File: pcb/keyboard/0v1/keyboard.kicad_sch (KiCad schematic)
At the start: 140 parts, among them SW1 A, SW10 A, SW11 A, SW12 A, SW13 A, SW14 A, SW15 A, SW16 A, SW17 A, SW18 A, SW19 A, SW2 A, SW20 A, SW21 A, SW22 A, SW23 A, SW24 A, SW25 A, SW26 A, SW27 A, SW28 A, SW29 A, SW3 A, SW30 A, SW31 A, SW32 A, SW33 A, SW34 A, SW35 A, SW36 A, SW37 A, SW38 A, SW39 A, SW4 A, SW40 A, SW41 A, SW42 A, SW43 A, SW44 A, SW45 A, SW46 A, SW47 A, SW48 A, SW49 A, SW5 A, SW50 A, SW51 A, SW52 A, SW53 A, SW54 A, SW55 A, SW56 A, SW57 A, SW58 A, SW59 A, SW6 A, SW60 A, SW61 A, SW62 A, SW63 A, SW7 A, SW8 A, SW9 A, U2 MDBT50Q-P1MV2, Y1 32.768

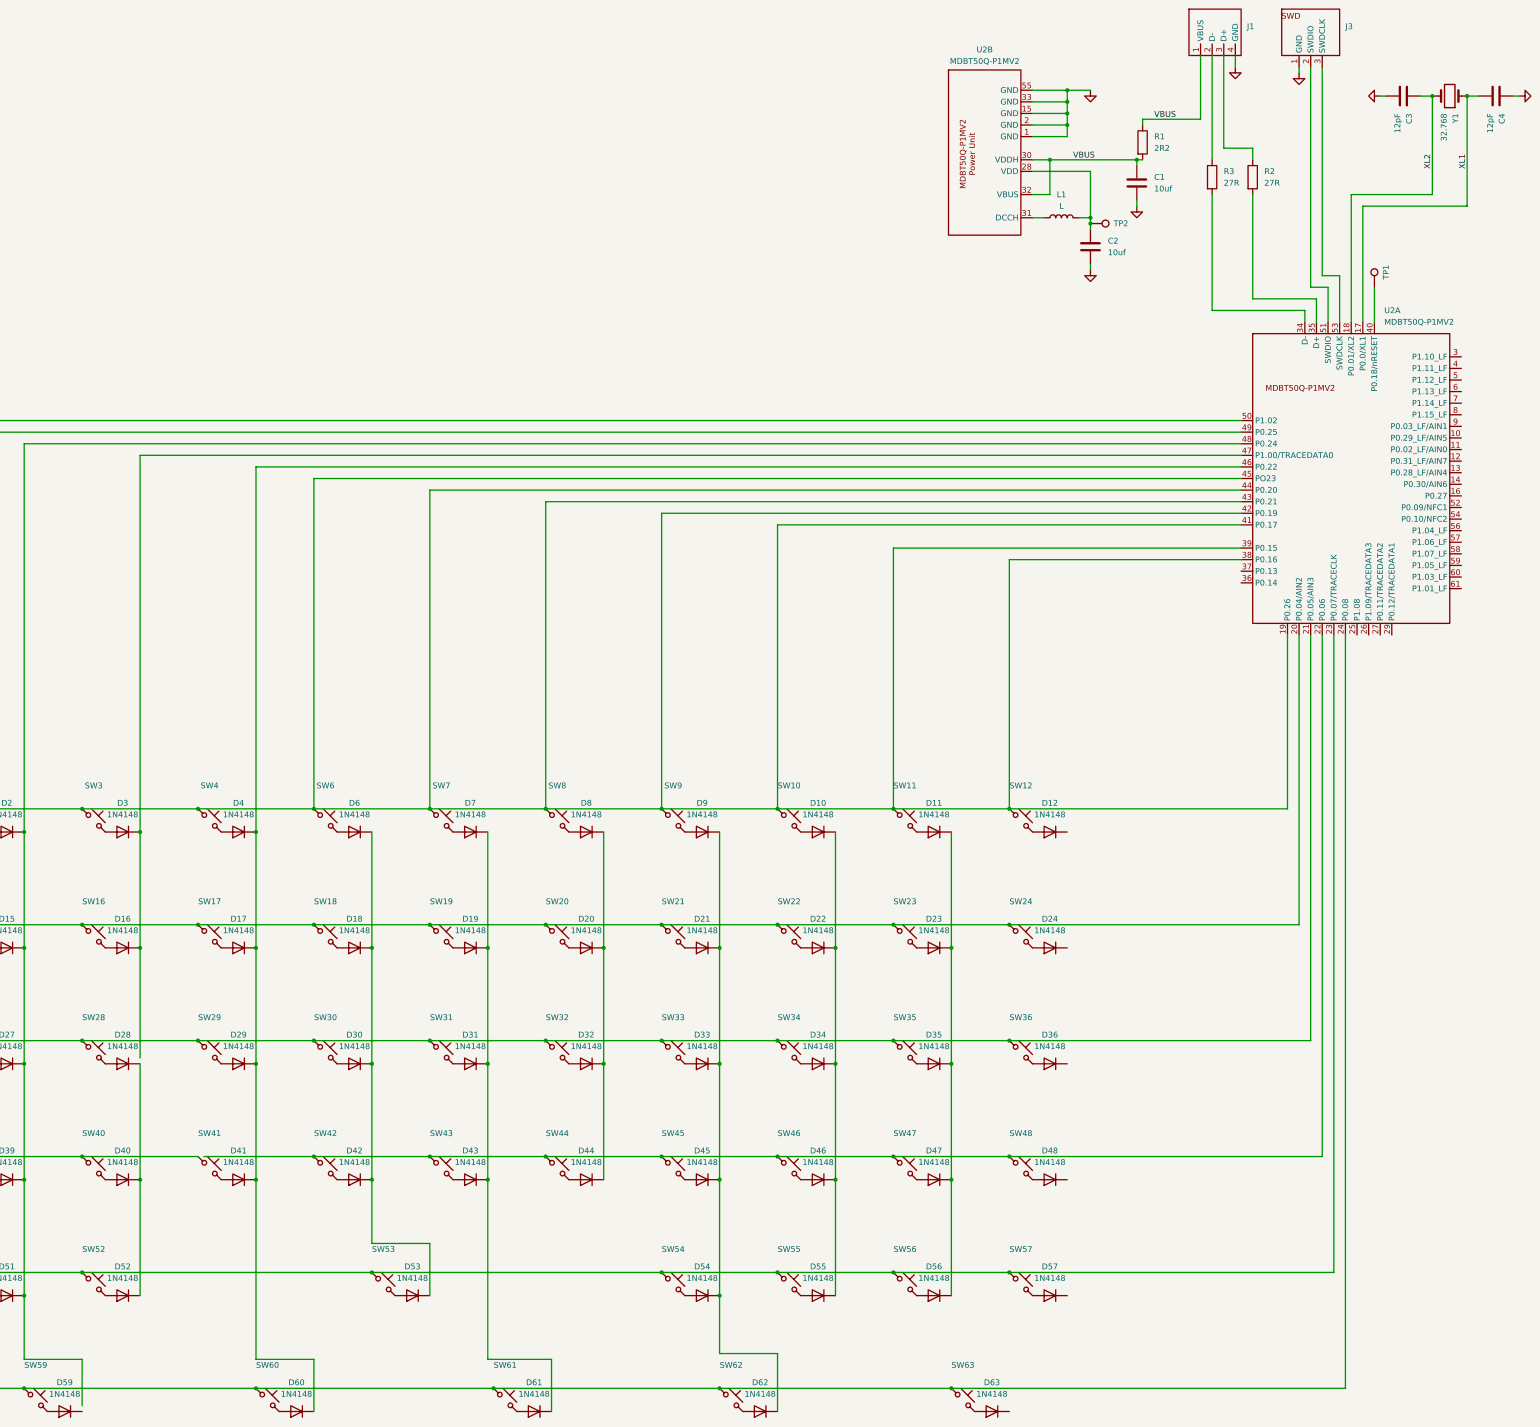
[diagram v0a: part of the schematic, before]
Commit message: Fix ERC errors in schematic editor
There were a few errors with the earlier design. Both real errors and
some just to make the ERC happy. These are fixed now, no errors and no
warnings.
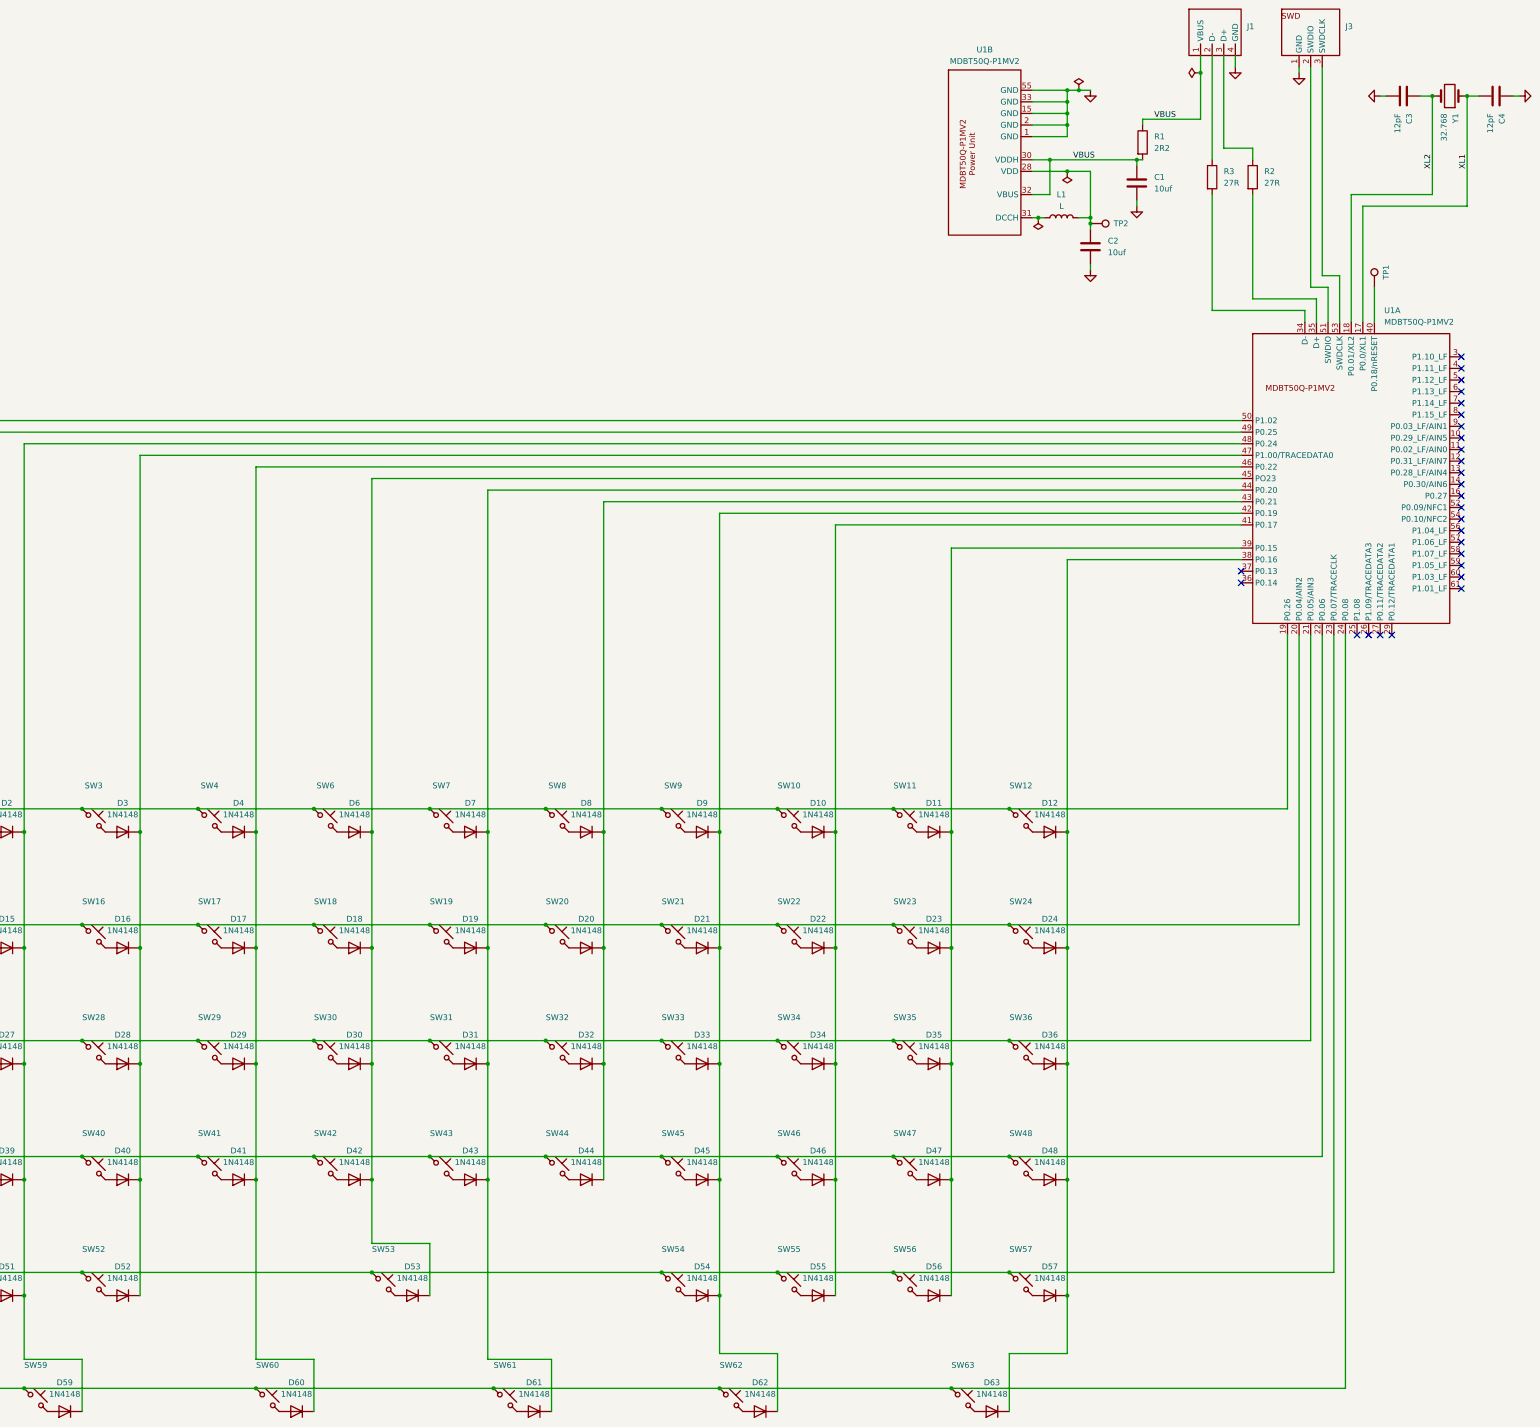
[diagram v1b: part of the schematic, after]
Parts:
- removed U2: MDBT50Q-P1MV2, symbol TH-A10C:MDBT50Q-P1MV2
- added U1: MDBT50Q-P1MV2, symbol TH-A10C:MDBT50Q-P1MV2
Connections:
- net GND: now also U1.1 (GND), U1.15 (GND), U1.2 (GND), U1.33 (GND), U1.55 (GND)
- net VBUS: now also U1.30 (VDDH), U1.32 (VBUS)
- net XL1: now also U1.17 (P0.0/XL1)
- net XL2: now also U1.18 (P0.01/XL2)
- net at SW13.1, SW14.1, SW15.1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: now also U1.20 (P0.04/AIN2)
- net at SW58.1, SW59.1, SW60.1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: now also U1.24 (P0.08)
- net at D15.1 (K), D2.1 (K), D27.1 (K)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: now also D59.1 (K), U1.48 (P0.24)
- net at D21.1 (K), D33.1 (K), D45.1 (K)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: now also U1.42 (P0.19)
- net at D1.1 (K), D14.1 (K), D26.1 (K)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: now also U1.49 (P0.25)
- net at SW37.1, SW38.1, SW39.1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: now also SW42.1, SW43.1, SW44.1, SW45.1, SW46.1, SW47.1, SW48.1, U1.22 (P0.06)
- net at SW25.1, SW26.1, SW27.1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: now also U1.21 (P0.05/AIN3)
- net at D13.1 (K), D25.1 (K), D37.1 (K)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: now also U1.50 (P1.02)
- net at D28.1 (K), D40.1 (K), D52.1 (K): now also D16.1 (K), D3.1 (K), U1.47 (P1.00/TRACEDATA0)
- net at D20.1 (K), D32.1 (K), D44.1 (K)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: now also U1.43 (P0.21)
- net at SW49.1, SW50.1, SW51.1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: now also U1.23 (P0.07/TRACECLK)
- net at SW1.1, SW10.1, SW11.1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: now also U1.19 (P0.26)
- net at D57.1 (K): now also D12.1 (K), D24.1 (K), D36.1 (K), D48.1 (K), D63.1 (K), U1.38 (P0.16)
- net at D11.1 (K), D23.1 (K), D35.1 (K)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: now also U1.39 (P0.15)
- net at D18.1 (K), D30.1 (K), D42.1 (K)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: now also U1.45 (PO23)
- net at D17.1 (K), D29.1 (K), D4.1 (K)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: now also U1.46 (P0.22)
- net at L1.1: now also U1.31 (DCCH)
- net at C2.1, L1.2, TP2.1: now also U1.28 (VDD)
- net at D19.1 (K), D31.1 (K), D43.1 (K)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: now also U1.44 (P0.20)
- net at D10.1 (K), D22.1 (K), D34.1 (K)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: now also U1.41 (P0.17)
- net at R3.2: now also U1.34 (D-)
- net at R2.2: now also U1.35 (D+)
- net at TP1.1: now also U1.40 (P0.18/nRESET)
- net at J3.2 (SWDIO): now also U1.51 (SWDIO)
- net at J3.3 (SWDCLK): now also U1.53 (SWDCLK)
- no-connect marks 0 -> 27
